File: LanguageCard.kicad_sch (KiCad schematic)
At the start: 29 parts, among them J1 Apple II Expansion Bus, U1 74LS86, U10 74LS06, U2 74LS08, U3 74LS175, U4 74LS32, U5 74LS08, U6 74LS08, U7 ROM F8, U8 6264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

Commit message: Update BOM
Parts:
- J1: now left out of the parts list
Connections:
- net ROM: now also JP1.2 (C), U10.11
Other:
- moved on the sheet: JP1
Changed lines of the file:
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@@
     (stroke (width 0) (type default) (color 0 0 0 0))
   )
-  (wire (pts (xy 189.23 85.09) (xy 191.77 85.09))
+  (wire (pts (xy 187.96 85.09) (xy 191.77 85.09))
     (stroke (width 0) (type default) (color 0 0 0 0))
   )
@@
     (effects (font (size 1.27 1.27)) (justify left bottom))
   )
-  (label "ROMCE" (at 185.42 78.74 180)
+  (label "ROMCE" (at 184.15 78.74 180)
     (effects (font (size 1.27 1.27)) (justify right bottom))
   )
@@
   )
   (symbol (lib_id "Apple II:Apple II Expansion Bus") (at 245.11 149.86 0) (unit 1)
-    (in_bom yes) (on_board yes)
+    (in_bom no) (on_board yes)
     (property "Reference" "J1" (id 0) (at 242.57 184.15 0))
     (property "Value" "Apple II Expansion Bus" (id 1) (at 245.11 182.6514 0))
@@
     (pin "2")
   )
-  (symbol (lib_id "Jumper:Jumper_3_Bridged12") (at 185.42 85.09 90) (mirror x) (unit 1)
-    (in_bom yes) (on_board yes) (fields_autoplaced)
-    (property "Reference" "JP1" (id 0) (at 182.88 83.8199 90)
+  (symbol (lib_id "Jumper:Jumper_3_Bridged12") (at 184.15 85.09 90) (mirror x) (unit 1)
+    (in_bom yes) (on_board yes) (fields_autoplaced)
+    (property "Reference" "JP1" (id 0) (at 181.61 83.8199 90)
       (effects (font (size 1.27 1.27)) (justify left))
     )
-    (property "Value" "ROM EN" (id 1) (at 182.88 86.3599 90)
+    (property "Value" "ROM EN" (id 1) (at 181.61 86.3599 90)
       (effects (font (size 1.27 1.27)) (justify left))
     )
-    (property "Footprint" "Connector_PinHeader_2.54mm:PinHeader_1x03_P2.54mm_Vertical" (id 2) (at 185.42 85.09 0)
-      (effects (font (size 1.27 1.27)) hide)
-    )
-    (property "Datasheet" "~" (id 3) (at 185.42 85.09 0)
+    (property "Footprint" "Connector_PinHeader_2.54mm:PinHeader_1x03_P2.54mm_Vertical" (id 2) (at 184.15 85.09 0)
+      (effects (font (size 1.27 1.27)) hide)
+    )
+    (property "Datasheet" "~" (id 3) (at 184.15 85.09 0)
       (effects (font (size 1.27 1.27)) hide)
     )
@@
     (pin "2")
   )
-  (symbol (lib_id "power:GND") (at 185.42 91.44 0) (mirror y) (unit 1)
-    (in_bom yes) (on_board yes) (fields_autoplaced)
-    (property "Reference" "#PWR017" (id 0) (at 185.42 97.79 0)
-      (effects (font (size 1.27 1.27)) hide)
-    )
-    (property "Value" "GND" (id 1) (at 187.96 92.7099 0)
+  (symbol (lib_id "power:GND") (at 184.15 91.44 0) (mirror y) (unit 1)
+    (in_bom yes) (on_board yes) (fields_autoplaced)
+    (property "Reference" "#PWR017" (id 0) (at 184.15 97.79 0)
+      (effects (font (size 1.27 1.27)) hide)
+    )
+    (property "Value" "GND" (id 1) (at 186.69 92.7099 0)
       (effects (font (size 1.27 1.27)) (justify right))
     )
-    (property "Footprint" "" (id 2) (at 185.42 91.44 0)
-      (effects (font (size 1.27 1.27)) hide)
-    )
-    (property "Datasheet" "" (id 3) (at 185.42 91.44 0)
-      (effects (font (size 1.27 1.27)) hide)
-    )
+    (property "Footprint" "" (id 2) (at 184.15 91.44 0)
+      (effects (font (size 1.27 1.27)) hide)
+    )
+    (property "Datasheet" "" (id 3) (at 184.15 91.44 0)
+      (effects (font (size 1.27 1.27)) hide)
+    )

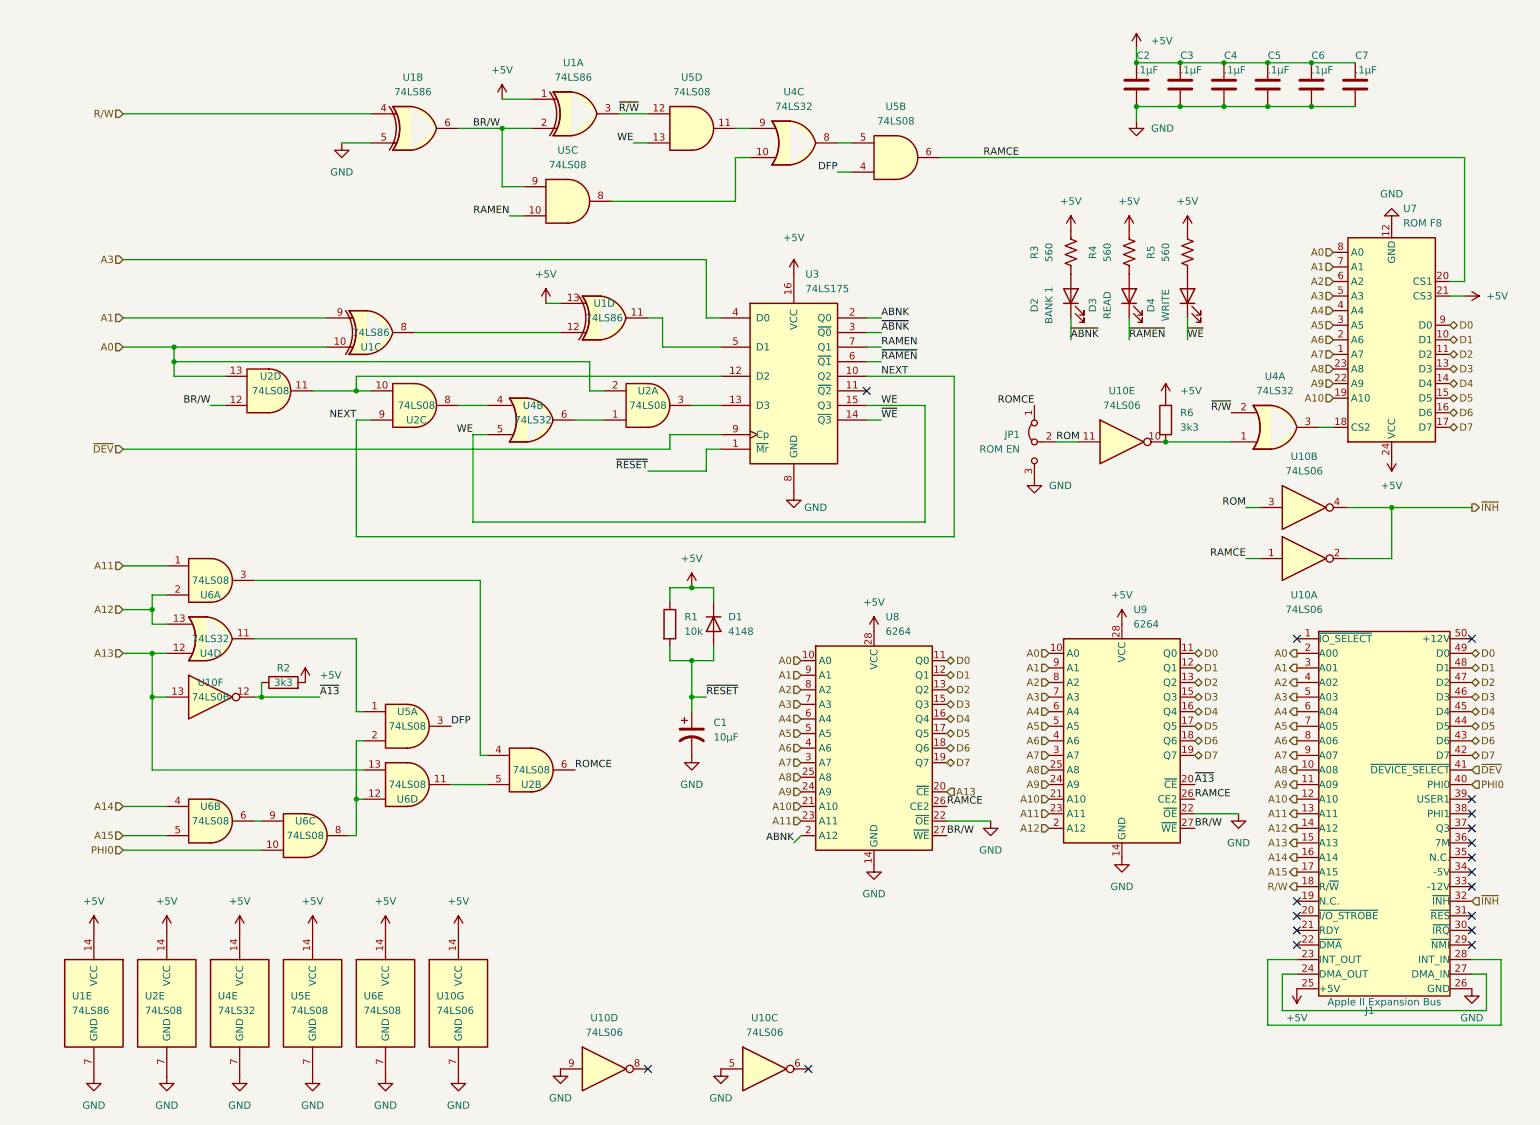
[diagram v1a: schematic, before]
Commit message: support larger SRAMS, minor updates
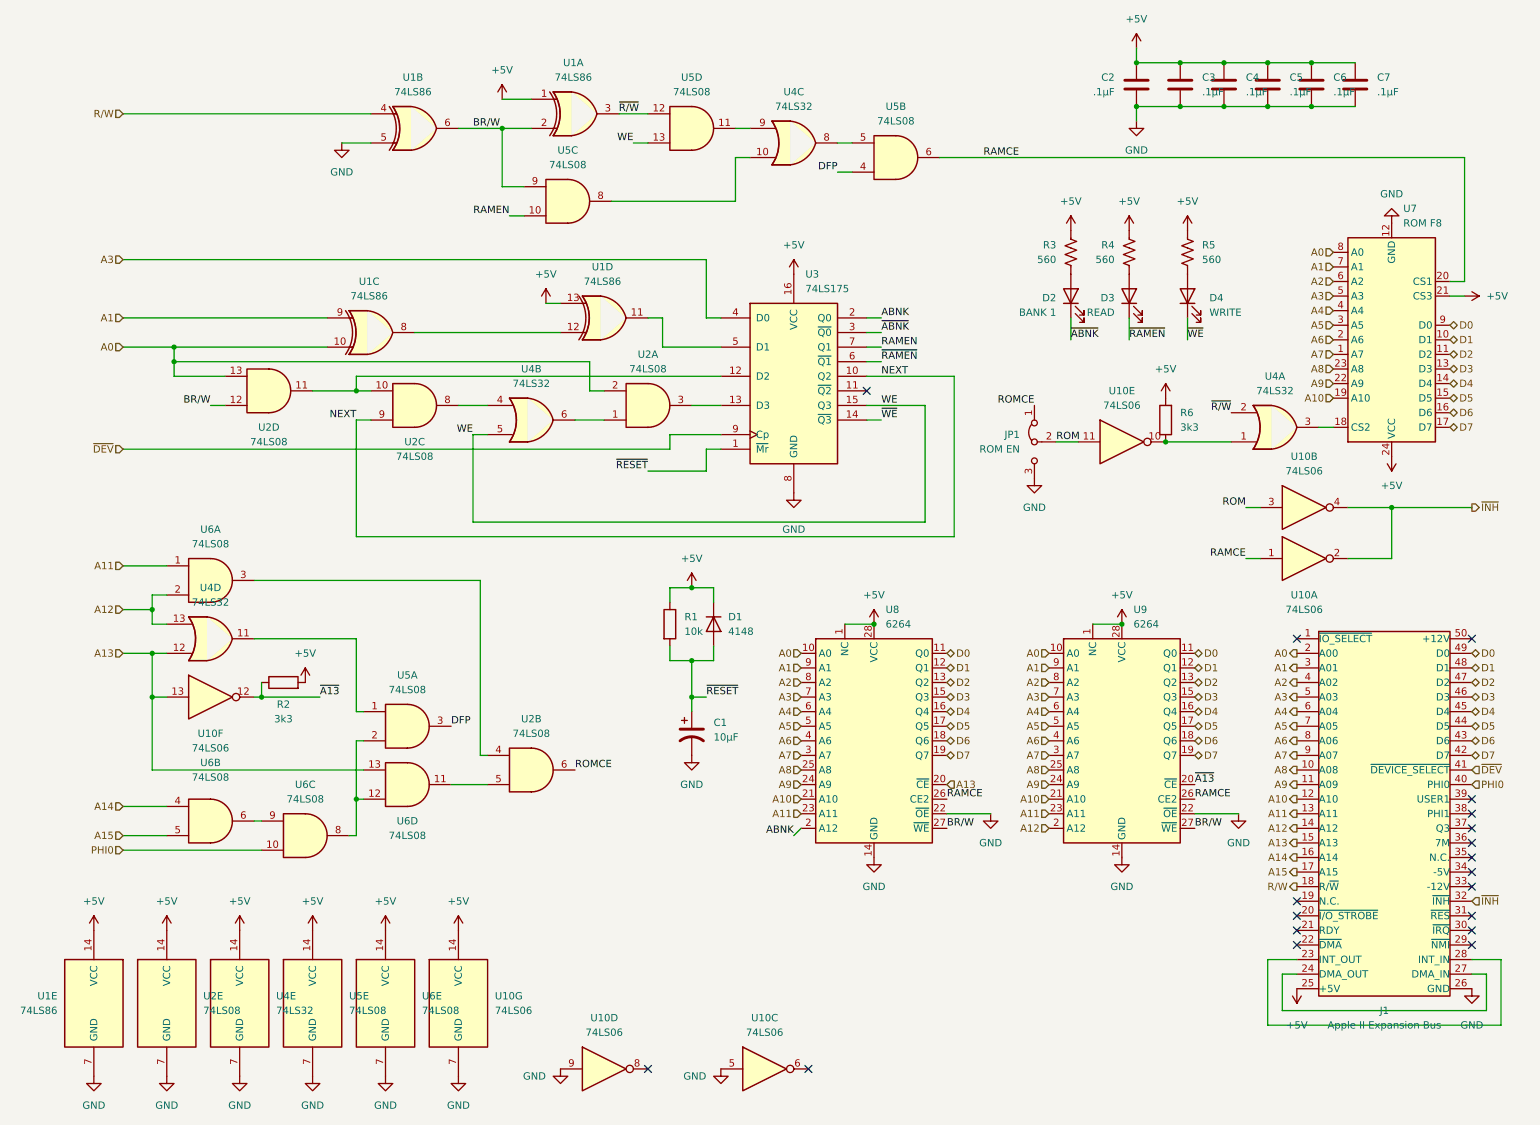
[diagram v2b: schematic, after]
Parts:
- R1, R2, R3, R4, R5, R6: footprint Resistor_THT:R_Axial_DIN0207_L6.3mm_D2.5mm_P7.62mm_Horizontal -> Resistor_THT:R_Axial_DIN0207_L6.3mm_D2.5mm_P10.16mm_Horizontal
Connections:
- net +5V: now also U8.1 (NC), U9.1 (NC)

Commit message: no, 32kx8 does not work. need two chip selects
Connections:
- net +5V: no longer U8.1 (NC), U9.1 (NC)
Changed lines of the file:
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@@
   (junction (at 232.41 26.67) (diameter 0) (color 0 0 0 0)
   )
-  (junction (at 156.21 116.84) (diameter 0) (color 0 0 0 0)
-  )
   (junction (at 30.48 129.54) (diameter 0) (color 0 0 0 0)
   )
@@
   )
   (junction (at 91.44 30.48) (diameter 0) (color 0 0 0 0)
-  )
-  (junction (at 199.39 116.84) (diameter 0) (color 0 0 0 0)
   )
   (junction (at 209.55 26.67) (diameter 0) (color 0 0 0 0)
@@
     (stroke (width 0) (type default) (color 0 0 0 0))
   )
-  (wire (pts (xy 194.31 116.84) (xy 199.39 116.84))
-    (stroke (width 0) (type default) (color 0 0 0 0))
-  )
   (wire (pts (xy 227.33 177.8) (xy 227.33 184.15))
     (stroke (width 0) (type default) (color 0 0 0 0))
@@
   )
   (wire (pts (xy 128.27 113.03) (xy 128.27 110.49))
-    (stroke (width 0) (type default) (color 0 0 0 0))
-  )
-  (wire (pts (xy 151.13 116.84) (xy 156.21 116.84))
     (stroke (width 0) (type default) (color 0 0 0 0))
   )
@@
     (pin "7")
   )
-  (symbol (lib_name "6264_1") (lib_id "MyRam:6264") (at 156.21 139.7 0) (unit 1)
+  (symbol (lib_id "MyRam:6264") (at 156.21 139.7 0) (unit 1)
     (in_bom yes) (on_board yes) (fields_autoplaced)
     (property "Reference" "U8" (id 0) (at 158.2294 114.3 0)
